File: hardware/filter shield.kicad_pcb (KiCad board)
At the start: 2 copper layers, 101.6 x 53.3 mm, 13 parts, among them J1 Screw_Terminal_01x03, J2 Screw_Terminal_01x03, J3 TR switch Connector, J6 Screw_Terminal_01x03, J7 Radioberry Connector, J8 BPF Connector, J9 LPF Connector, P10 CONN_01X01, P11 CONN_01X01, P13 CONN_01X01, P8 CONN_01X01, U1 BOB-12009

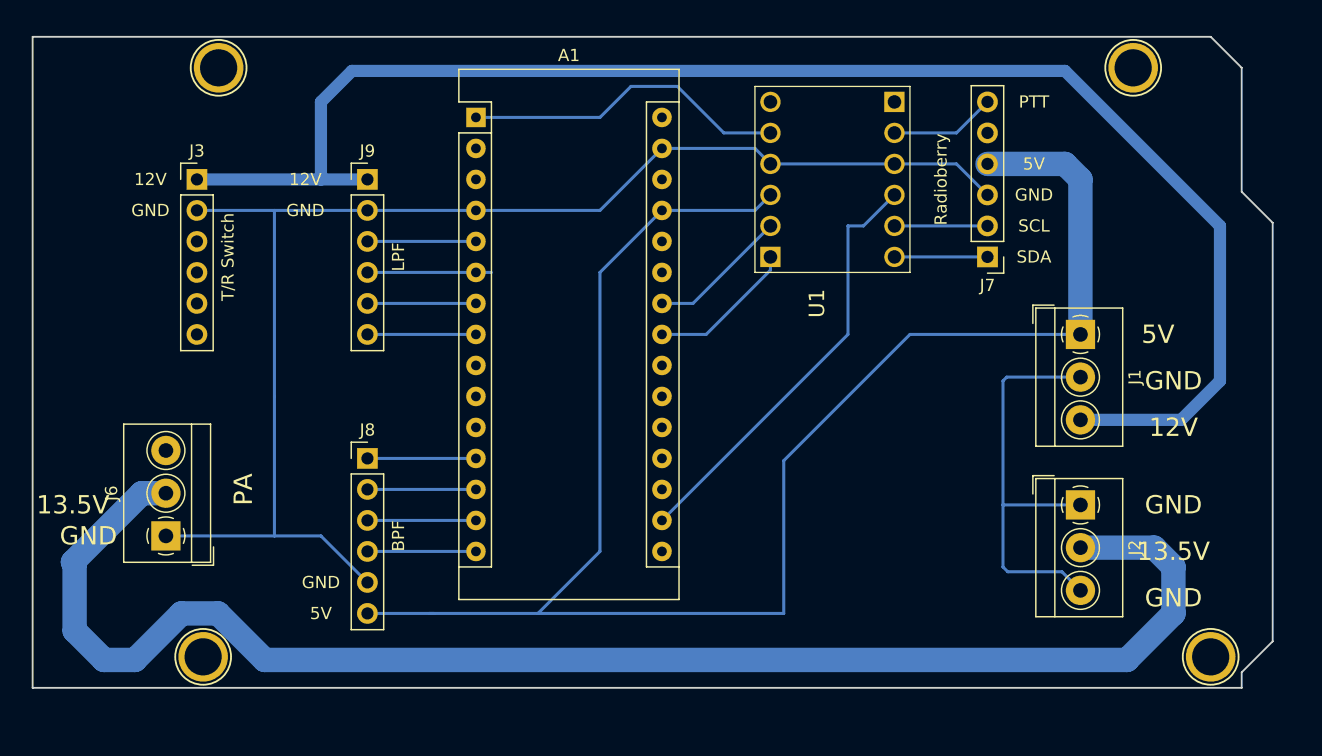
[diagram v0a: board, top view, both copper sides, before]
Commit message: tr switch circuit added
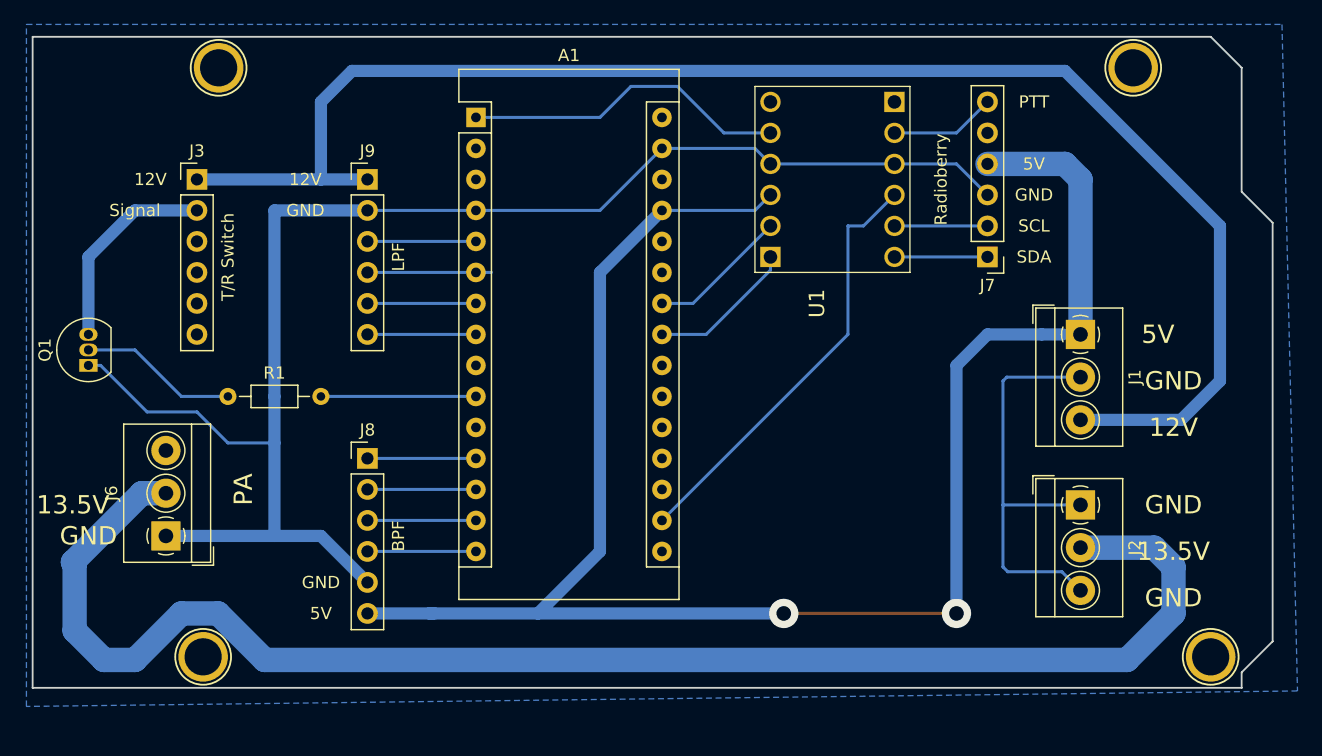
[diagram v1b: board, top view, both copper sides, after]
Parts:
- added Q1: PN2222A, Package_TO_SOT_THT:TO-92_Inline, F.Cu at (108.0, 95.2)
- added R1: 14k, Resistor_THT:R_Axial_DIN0204_L3.6mm_D1.6mm_P7.62mm_Horizontal, F.Cu at (119.4, 97.8)
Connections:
- A1 pad 10: Net-(A1-Pad10) -> /txmit
- A1 pad 11: /txmit -> Net-(A1-Pad11)
- J3 pad 2: GND -> Net-(J3-Pad2)
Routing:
- net Net-(J3-Pad2): track 0.00 -> 16.8 mm
- net Net-(Q1-Pad2): track 0.00 -> 13.0 mm
- net /txmit: track 0.00 -> 12.7 mm
- net GND: track 148.4 -> 159.9 mm
- net +5V: track 144.6 -> 147.7 mm, vias 0 -> 2
- added copper zone on B.Cu, net GND
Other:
- board text added: "Signal"

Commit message: First version completed and ready to etch.
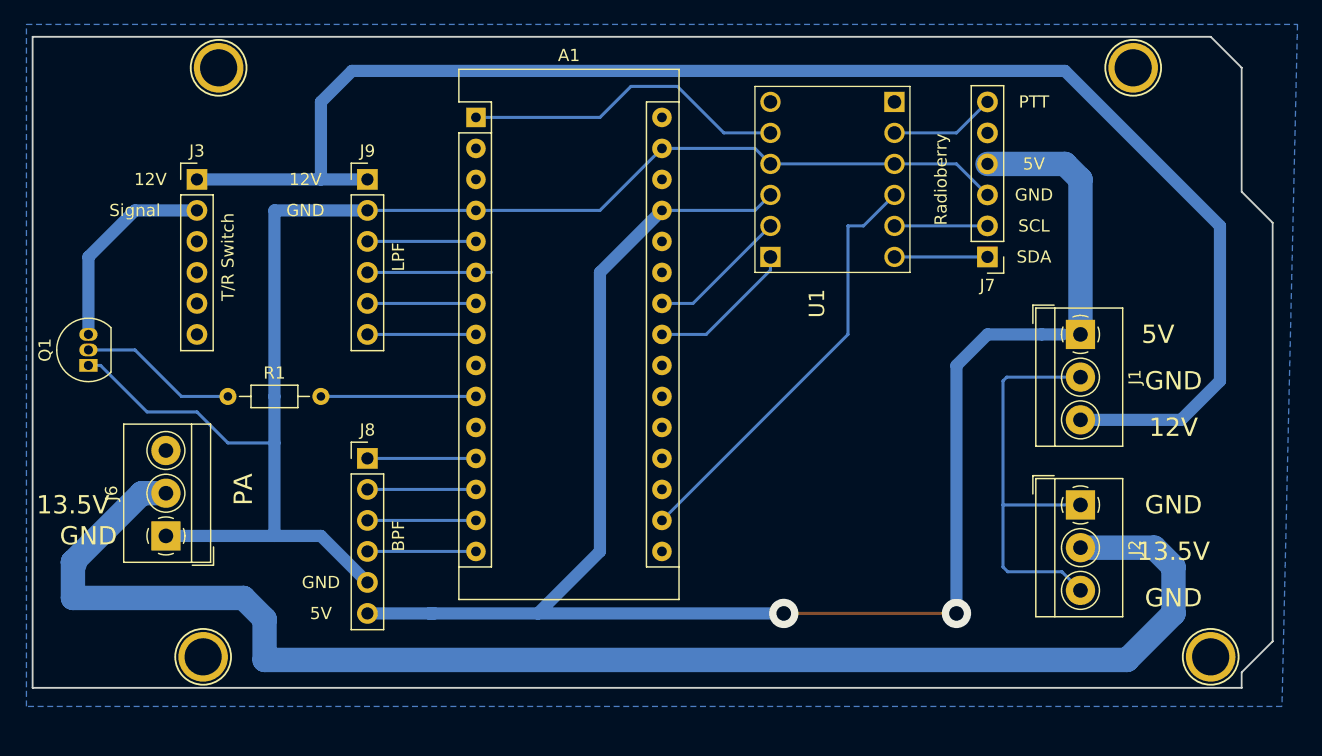
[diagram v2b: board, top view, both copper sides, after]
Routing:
- net +15V: track 123.5 -> 121.0 mm
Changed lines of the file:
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@@
     (thickness 1.6)
     (drawings 33)
-    (tracks 106)
+    (tracks 104)
     (zones 0)
     (modules 15)
@@
   )
   (setup
-    (last_trace_width 0.25)
+    (last_trace_width 2)
     (user_trace_width 1)
     (user_trace_width 2)
@@
   (segment (start 106.68 111.362946) (end 112.322946 105.72) (width 2) (layer B.Cu) (net 8))
   (segment (start 193.04 119.38) (end 122.385362 119.38) (width 2) (layer B.Cu) (net 8))
-  (segment (start 111.76 119.38) (end 109.22 119.38) (width 2) (layer B.Cu) (net 8))
   (segment (start 106.819999 111.502945) (end 106.68 111.362946) (width 2) (layer B.Cu) (net 8))
-  (segment (start 109.22 119.38) (end 106.819999 116.979999) (width 2) (layer B.Cu) (net 8))
-  (segment (start 118.575362 115.57) (end 115.57 115.57) (width 2) (layer B.Cu) (net 8))
   (segment (start 196.85 115.57) (end 193.04 119.38) (width 2) (layer B.Cu) (net 8))
   (segment (start 196.85 111.76) (end 196.85 115.57) (width 2) (layer B.Cu) (net 8))
   (segment (start 189.23 110.18) (end 195.27 110.18) (width 2) (layer B.Cu) (net 8))
   (segment (start 195.27 110.18) (end 196.85 111.76) (width 2) (layer B.Cu) (net 8))
-  (segment (start 106.819999 116.979999) (end 106.819999 111.502945) (width 2) (layer B.Cu) (net 8))
-  (segment (start 122.385362 119.38) (end 118.575362 115.57) (width 2) (layer B.Cu) (net 8))
-  (segment (start 115.57 115.57) (end 111.76 119.38) (width 2) (layer B.Cu) (net 8))
+  (segment (start 106.68 111.362946) (end 106.68 114.3) (width 2) (layer B.Cu) (net 8))
+  (segment (start 106.68 114.3) (end 120.65 114.3) (width 2) (layer B.Cu) (net 8))
+  (segment (start 122.385362 116.035362) (end 122.385362 119.38) (width 2) (layer B.Cu) (net 8))
+  (segment (start 120.65 114.3) (end 122.385362 116.035362) (width 2) (layer B.Cu) (net 8))
   (segment (start 200.66 96.52) (end 197.47 99.71) (width 1) (layer B.Cu) (net 9))
   (segment (start 200.66 83.82) (end 200.66 96.52) (width 1) (layer B.Cu) (net 9))
@@
   (segment (start 111.76 93.98) (end 115.57 97.79) (width 0.25) (layer B.Cu) (net 48))
   (zone (net 1) (net_name GND) (layer B.Cu) (hatch edge 0.508)
-    (connect_pads (clearance 0.508))
+    (connect_pads (clearance 0.5))
     (min_thickness 0.254)
     (fill yes (arc_segments 32) (thermal_gap 0.508) (thermal_bridge_width 0.508))
     (polygon
       (pts
-        (xy 207.01 121.92) (xy 102.87 123.19) (xy 102.87 67.31) (xy 205.74 67.31)
+        (xy 205.74 123.19) (xy 102.87 123.19) (xy 102.87 67.31) (xy 207.01 67.31)
       )
     )

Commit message: Small corrections
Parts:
- added Q2: PN2222A, Package_TO_SOT_THT:TO-92_Inline, F.Cu at (111.8, 91.4)
- added R2: 14k, Resistor_THT:R_Axial_DIN0204_L3.6mm_D1.6mm_P7.62mm_Horizontal, F.Cu at (119.4, 95.2)
- moved Q1 10.9 mm to (111.8, 85.1)
- moved J3 2.54 mm to (119.4, 80.0)
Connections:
- A1 pad 9: Net-(A1-Pad9) -> /pa
- J3 pad 3: Net-(J3-Pad3) -> GND
- J3 pad 5: Net-(J3-Pad5) -> GND
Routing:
- net Net-(Q2-Pad2): track 0.00 -> 20.6 mm
- net Net-(Q1-Pad2): track 13.0 -> 32.8 mm
- net /pa: track 0.00 -> 12.7 mm
- net Net-(J3-Pad2): track 16.8 -> 7.62 mm
- net Net-(J3-Pad4): track 0.00 -> 8.15 mm
- net +3V3: track 35.3 -> 42.7 mm
- net GND: track 159.9 -> 165.5 mm
- net /scl: track 11.5 -> 13.0 mm
- net +12V: track 125.7 -> 124.3 mm
- net /ptt: track 26.8 -> 27.5 mm
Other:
- board text added: "10m"
- board text added: "20m"
- board text added: "40m"
- board text added: "80m"
- board text added: "Radioberry Filters Companion VA2SAJ V0.1"
- board text added: "T/R Switch - PA"
- board text added: "p1"
- board text added: "p2"
- board text added: "p3"
- board text added: "p4"
- board text added: "pa sig"
- board text added: "tx sig"
- board text removed: "T/R Switch"
